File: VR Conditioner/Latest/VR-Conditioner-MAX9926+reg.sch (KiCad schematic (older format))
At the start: 22 parts, among them J1 8-pin header, J2 Edge, U1 MAX9926UAEE+, U2 AMS1117CD-5.0

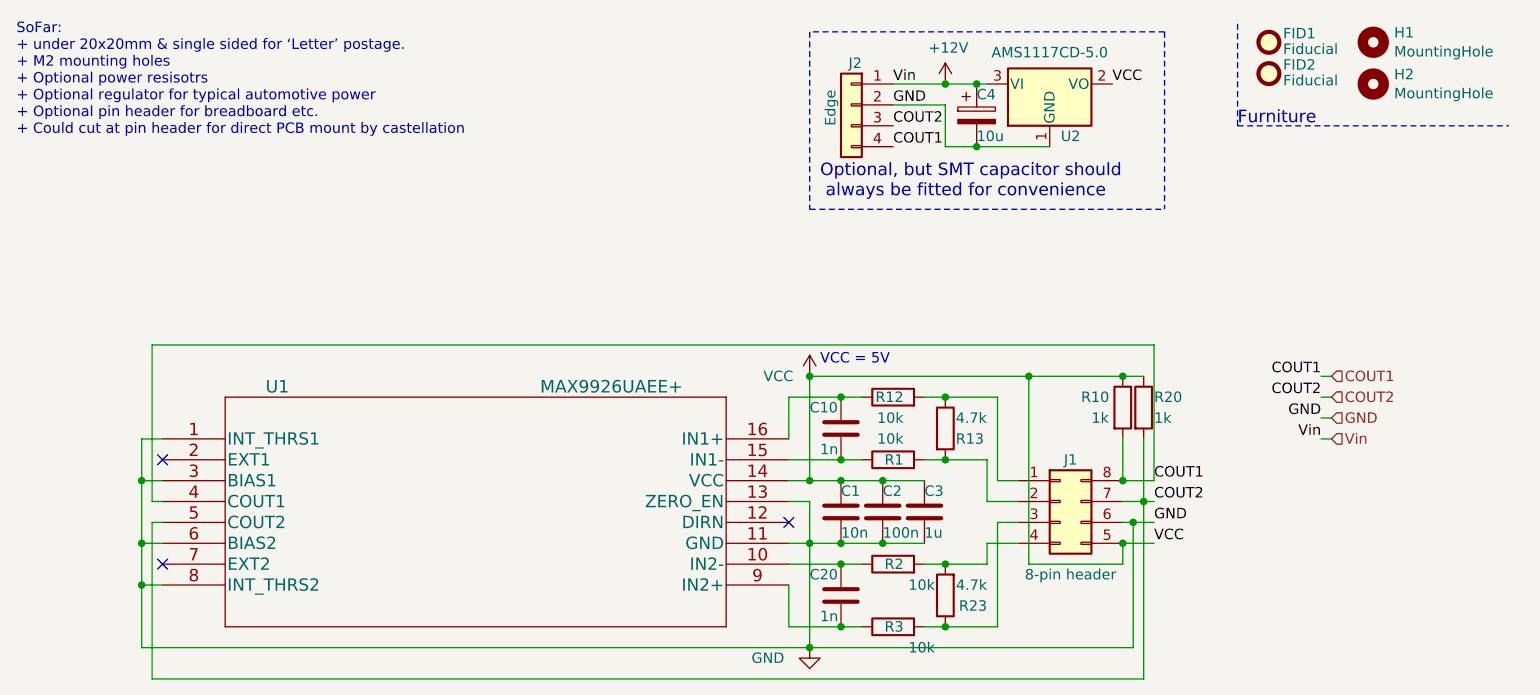
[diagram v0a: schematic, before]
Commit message: Improve silk screen labeling & ground plane. Added solder pads.
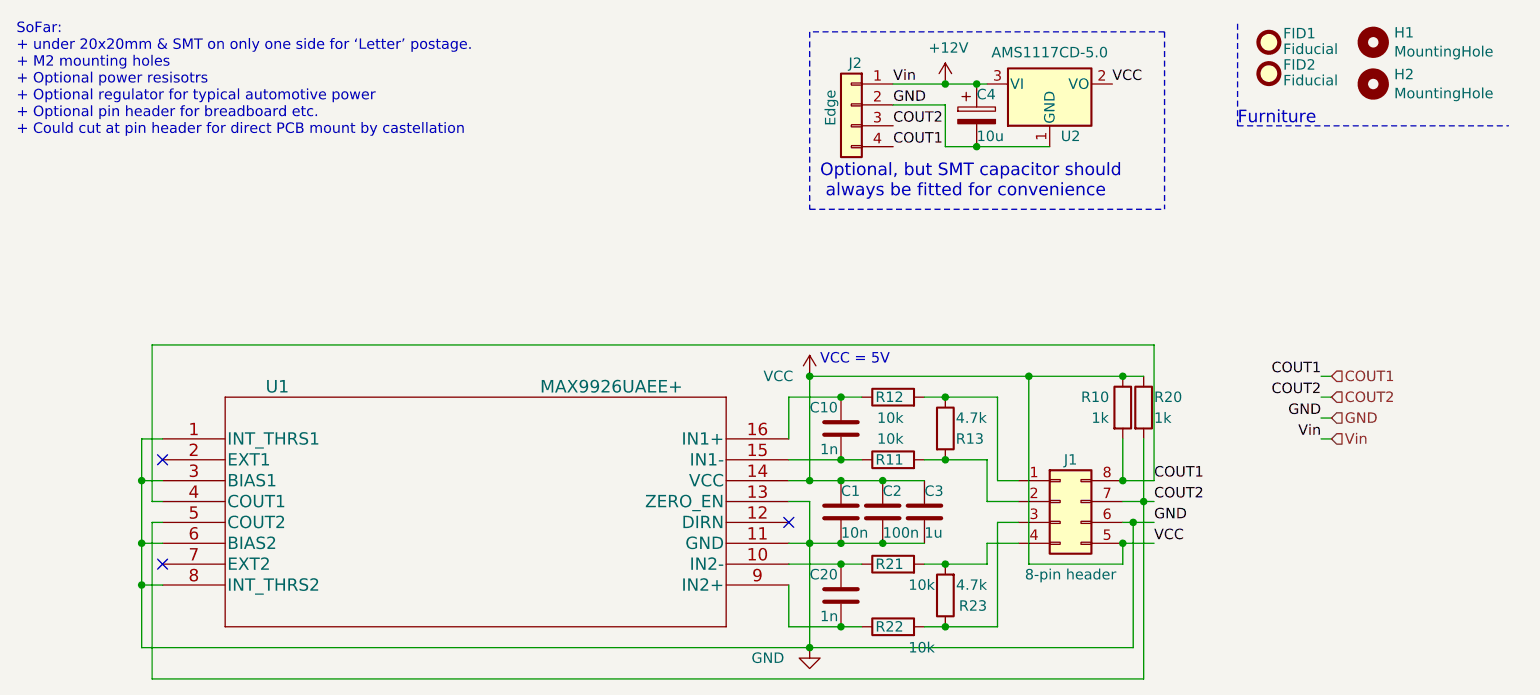
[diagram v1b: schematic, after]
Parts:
- renumbered R1 to R11, R2 to R21, R3 to R22
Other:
- note added: "SoFar:\n+ under 20x20mm & SMT on only one side for ‘Letter’ postage.\n+ M2 mounting holes\n+ Optional power resisotrs\n+ Optional regulator for typical automotive power\n+ Optional pin header for breadboard etc. \n+ Could cut at pin header for direct PCB mount by castellation"
- note removed: "SoFar:\n+ under 20x20mm & single sided for ‘Letter’ postage.\n+ M2 mounting holes\n+ Optional power resisotrs\n+ Optional regulator for typical automotive power\n+ Optional pin header for breadboard etc. \n+ Could cut at pin header for direct PCB mount by castellation"
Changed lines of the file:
@@
 Sheet 1 1
 Title "Dual Variable Reluctance MAX9926 mode A2"
-Date "2021-02-24"
-Rev "3.5"
+Date "2021-08-16"
+Rev "3.7"
 Comp "(c)2021 Phill Rogers @ TechColab.co.je"
 Comment1 "Optional onboard regulator or 5V direct"
@@
 Connection ~ 5900 3000
 Text Notes 600  1050 0    50   ~ 0
-SoFar:\n+ under 20x20mm & single sided for ‘Letter’ postage.\n+ M2 mounting holes\n+ Optional power resisotrs\n+ Optional regulator for typical automotive power\n+ Optional pin header for breadboard etc. \n+ Could cut at pin header for direct PCB mount by castellation
+SoFar:\n+ under 20x20mm & SMT on only one side for ‘Letter’ postage.\n+ M2 mounting holes\n+ Optional power resisotrs\n+ Optional regulator for typical automotive power\n+ Optional pin header for breadboard etc. \n+ Could cut at pin header for direct PCB mount by castellation
 Text Label 6850 2200 2    50   ~ 0
 COUT1
@@
 	6850 2500 6900 2500
 $Comp
-L Device:R R3
+L Device:R R22
 U 1 1 60812326
 P 4800 3400
-F 0 "R3" V 4800 3350 50  0000 L CNN
+F 0 "R22" V 4800 3350 50  0000 L CNN
 F 1 "10k" V 4700 3200 50  0000 L CNN
 F 2 "Resistor_SMD:R_1206_3216Metric" V 4730 3400 50  0001 C CNN
@@
 $EndComp
 $Comp
-L Device:R R2
+L Device:R R21
 U 1 1 6081295A
 P 4800 3100
-F 0 "R2" V 4800 3050 50  0000 L CNN
+F 0 "R21" V 4800 3050 50  0000 L CNN
 F 1 "10k" V 4700 2900 50  0000 L CNN
 F 2 "Resistor_SMD:R_1206_3216Metric" V 4730 3100 50  0001 C CNN
@@
 $EndComp
 $Comp
-L Device:R R1
+L Device:R R11
 U 1 1 60812D66
 P 4800 2600
-F 0 "R1" V 4800 2550 50  0000 L CNN
+F 0 "R11" V 4800 2550 50  0000 L CNN
 F 1 "10k" V 4900 2550 50  0000 L CNN
 F 2 "Resistor_SMD:R_1206_3216Metric" V 4730 2600 50  0001 C CNN
